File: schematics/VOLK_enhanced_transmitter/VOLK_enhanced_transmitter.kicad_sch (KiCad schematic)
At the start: 7 parts, among them J1 AudioJack3, Q1 IRF3205

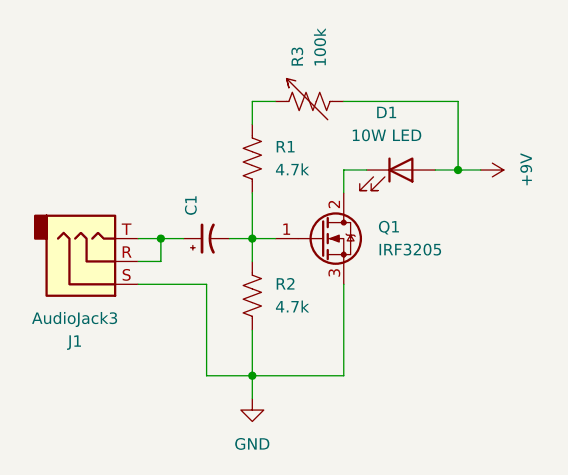
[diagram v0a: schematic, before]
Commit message: changed MCU pin assignments and added schematics for MCU enhanced circuits
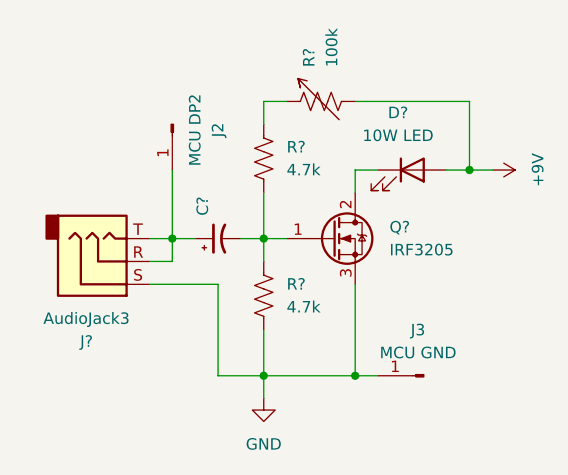
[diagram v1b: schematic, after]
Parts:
- removed D1: 10W LED, symbol Device:LED
- removed J1: AudioJack3, symbol Connector_Audio:AudioJack3
- removed Q1: IRF3205, Package_TO_SOT_THT:TO-220-3_Vertical, symbol Transistor_FET:IRF3205
- removed R2: 4.7k, symbol Device:R_US
- added D?: 10W LED, symbol Device:LED
- added J2: MCU DP2, symbol Connector:Conn_01x01_Pin
- added J3: MCU GND, symbol Connector:Conn_01x01_Pin
- added J?: AudioJack3, symbol Connector_Audio:AudioJack3
- added Q?: IRF3205, Package_TO_SOT_THT:TO-220-3_Vertical, symbol Transistor_FET:IRF3205
- added R?: 4.7k, symbol Device:R_US
- renumbered C1 to C?, R1 to R?, R3 to R?
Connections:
- net +9V: now also D?.2 (A)
- net GND: now also J3.1 (Pin_1), J?.S, Q?.3 (S), R?.2
- net at C?.1: now also J2.1 (Pin_1), J?.R, J?.T
- net at C?.2, R?.2: now also Q?.1 (G), R?.1
- new net: D?.1 (K), Q?.2 (D)
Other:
- title: VOLF Passive Transmitter -> VOLF Enhanced Transmitter
- moved on the sheet: C?, R?
